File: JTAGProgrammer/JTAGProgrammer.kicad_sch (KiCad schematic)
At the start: 7 parts, among them J1 USB_B_Micro, J5 Conn_01x03

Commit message: Add LCSC part numbers
Signed-off-by: Anthony Bernaert <anthony.bernaert@gmail.com>
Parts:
- J1: LCSC (none) -> C132563
- J5: LCSC (none) -> C146243
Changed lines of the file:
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@@
+      (effects (font (size 1.27 1.27)) hide)
+    )
+    (property "LCSC" "C146243" (at 215.9 134.62 0)
       (effects (font (size 1.27 1.27)) hide)
     )
@@
       (effects (font (size 1.27 1.27)) hide)
     )
+    (property "LCSC" "C132563" (at 58.42 74.295 0)
+      (effects (font (size 1.27 1.27)) hide)
+    )

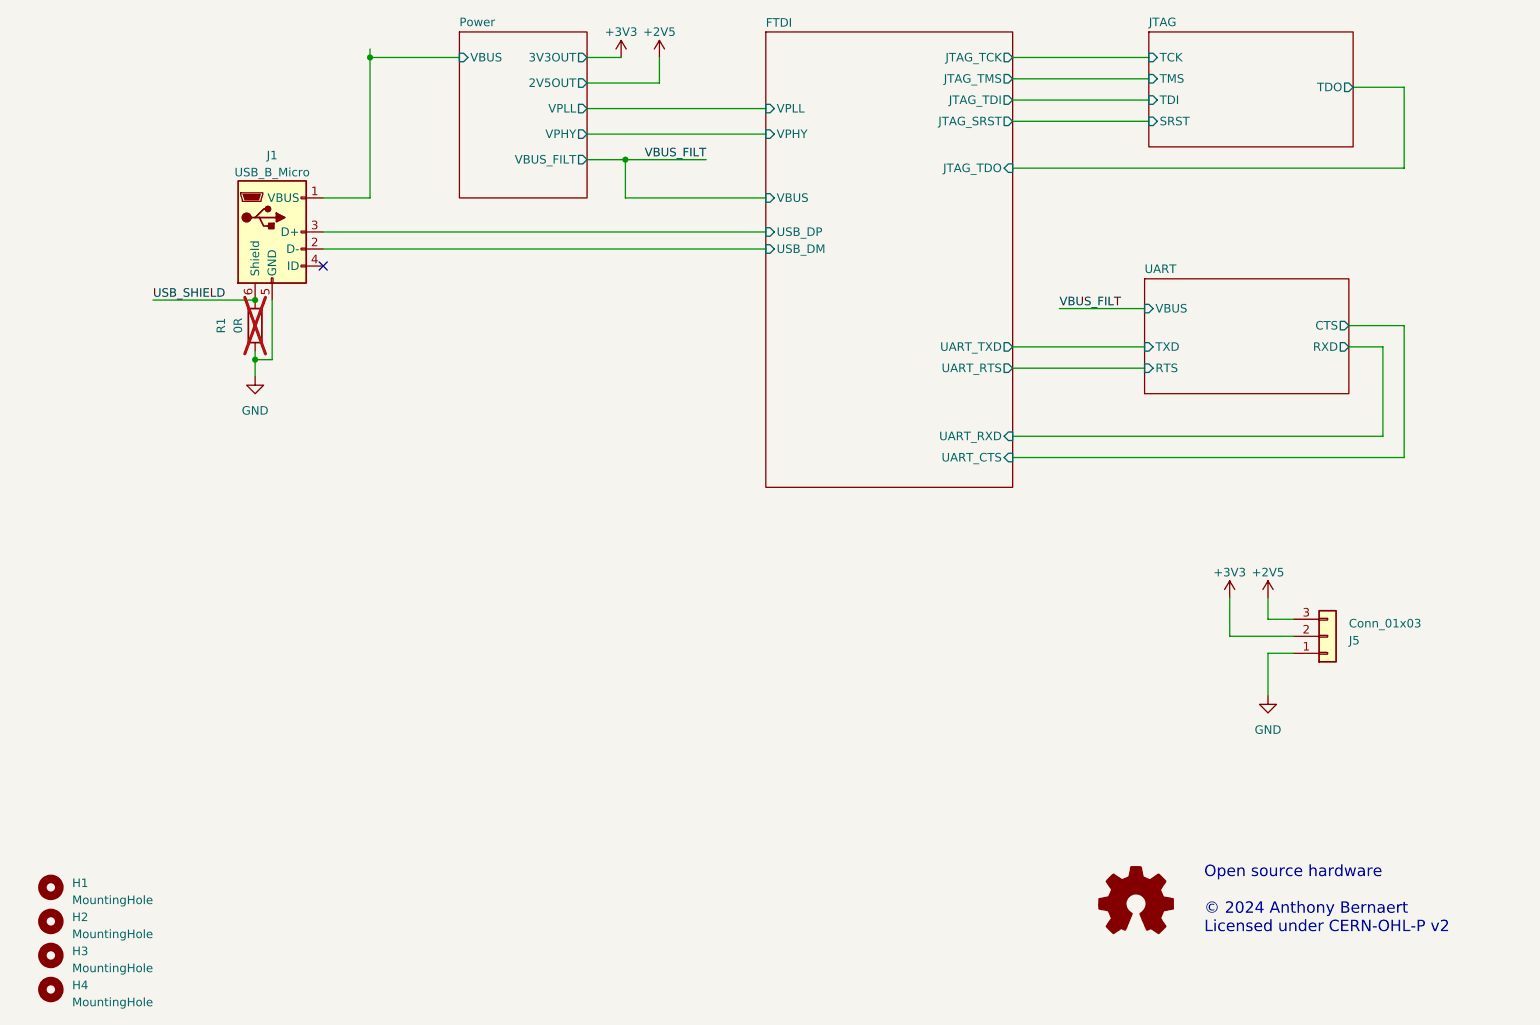
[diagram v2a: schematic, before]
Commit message: Rev.2: change to USB Type-C, add VBUS fuse, VREF LED indicators
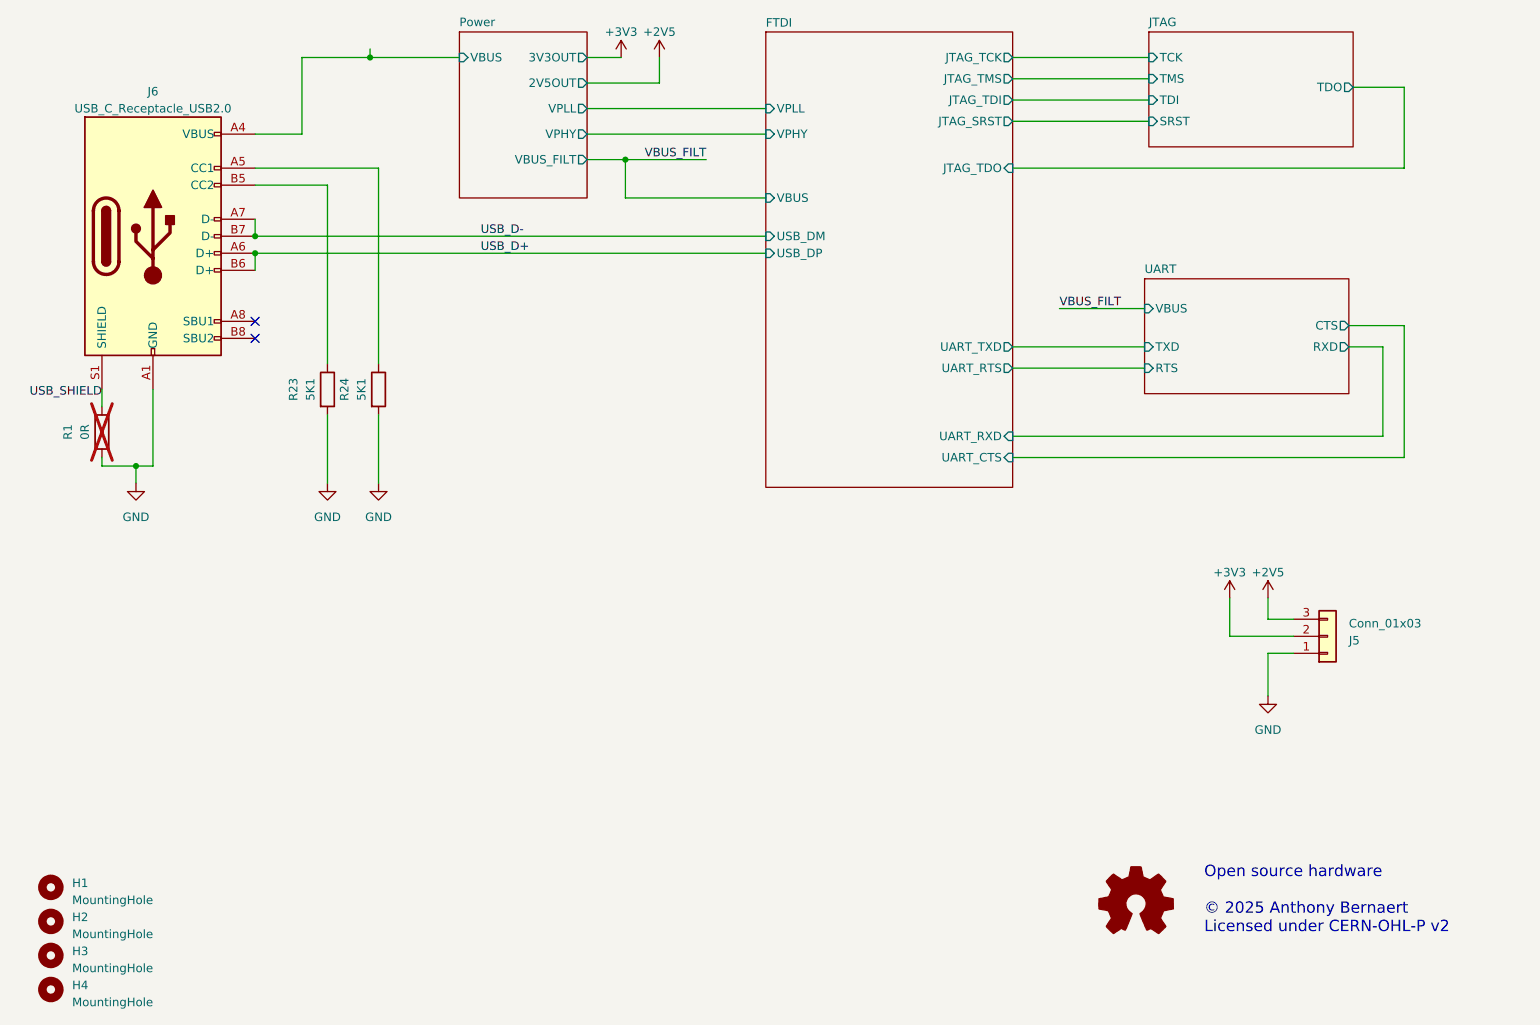
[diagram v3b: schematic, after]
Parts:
- removed J1: USB_B_Micro, Connector_USB:USB_Micro-B_Amphenol_10118194_Horizontal, symbol Connector:USB_B_Micro
- added J6: USB_C_Receptacle_USB2.0, Connector_USB:USB_C_Receptacle_GCT_USB4105-xx-A_16P_TopMnt_Horizontal, symbol Connector:USB_C_Receptacle_USB2.0
- added R23, R24: 5K1, Resistor_SMD:R_0603_1608Metric, symbol Device:R
- R1: now left out of the parts list
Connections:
- net GND: now also J6.A1 (GND), J6.A12 (GND), J6.B1 (GND), J6.B12 (GND), R23.2, R24.2
- net Power/VBUS: now also J6.A4 (VBUS), J6.A9 (VBUS), J6.B4 (VBUS), J6.B9 (VBUS)
- net USB_SHIELD: now also J6.S1 (SHIELD)
- new net: J6.B5 (CC2), R23.1
- new net: J6.A5 (CC1), R24.1
- new net USB_D+: J6.A6 (D+), J6.B6 (D+)
- new net USB_D-: J6.A7 (D-), J6.B7 (D-)
- no-connect marks 1 -> 2
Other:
- note added: "Open source hardware © 2025 Anthony Bernaert Licensed under CERN-OHL-P v2"
- note removed: "Open source hardware © 2024 Anthony Bernaert Licensed under CERN-OHL-P v2"
- moved on the sheet: R1
